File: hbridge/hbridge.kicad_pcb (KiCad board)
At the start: 2 copper layers, 53.3 x 31.8 mm, 22 parts, among them J1 CONN_A, J2 CONN_B, J3 CONN_MOTOR, J4 CONN_POWER, Q1 TIP120, Q2 TIP120, Q3 TIP120, Q4 TIP120, U1 OPTO-TRANSISTOR, U2 OPTO-TRANSISTOR

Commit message: hbridge: First PCB made
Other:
- net class Default: via_dia 1 -> 0.1; via_drill 0.1 -> 0.05
- rule via_min_drill: 0.1 -> 0.01
- rule via_min_size: 0.4 -> 0.01
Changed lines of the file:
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@@
     (links 24)
     (no_connects 0)
-    (area 0 0 0 0)
+    (area 114.070001 74.77 182.726 138.676)
     (thickness 1.6)
     (drawings 6)
@@
     (segment_width 0.2)
     (edge_width 0.15)
-    (via_size 1)
-    (via_drill 0.1)
-    (via_min_size 0.4)
-    (via_min_drill 0.1)
+    (via_size 0.1)
+    (via_drill 0.05)
+    (via_min_size 0.01)
+    (via_min_drill 0.01)
     (uvia_size 0.3)
     (uvia_drill 0.1)
@@
     (mod_text_size 1 1)
     (mod_text_width 0.15)
-    (pad_size 1.524 1.524)
-    (pad_drill 0.762)
+    (pad_size 4.064 4.064)
+    (pad_drill 0)
     (pad_to_mask_clearance 0.2)
     (aux_axis_origin 0 0)
@@
       (drillshape 0)
       (scaleselection 1)
-      (outputdirectory ""))
+      (outputdirectory ../export/))
   )
   (net 0 "")
@@
     (clearance 0.381)
     (trace_width 0.381)
-    (via_dia 1)
-    (via_drill 0.1)
+    (via_dia 0.1)
+    (via_drill 0.05)
     (uvia_dia 0.3)
     (uvia_drill 0.1)
@@
     (fp_circle (center 0 0) (end 2.6 0) (layer F.CrtYd) (width 0.05))
     (fp_circle (center 0 0) (end 0 -2.286) (layer F.SilkS) (width 0.12))
-    (pad 1 thru_hole circle (at 0 0) (size 4.064 4.064) (drill 3.2) (layers *.Cu *.Mask))
+    (pad 1 smd circle (at 0 0) (size 4.064 4.064) (layers B.Cu F.Paste F.Mask))
   )
   (module Resistors_SMD:R_1210 (layer F.Cu)
@@
   (segment (start 135.89 110.31) (end 136.07 110.31) (width 0.381) (layer F.Cu) (net 2))
   (segment (start 130.81 102.87) (end 130.81 95.25) (width 0.381) (layer F.Cu) (net 3))
-  (via (at 148.59 95.25) (size 1) (drill 0.1) (layers F.Cu B.Cu) (net 3) (status 30))
+  (via (at 148.59 95.25) (size 0.1) (drill 0.05) (layers F.Cu B.Cu) (net 3) (status 30))
   (segment (start 148.59 95.25) (end 152.4 95.25) (width 0.381) (layer F.Cu) (net 3) (status 10))
   (segment (start 130.81 95.25) (end 140.97 95.25) (width 0.381) (layer F.Cu) (net 3))
   (segment (start 140.97 95.25) (end 146.05 95.25) (width 0.381) (layer F.Cu) (net 3) (status 20))
-  (via (at 146.05 95.25) (size 1) (drill 0.1) (layers F.Cu B.Cu) (net 3) (status 30))
+  (via (at 146.05 95.25) (size 0.1) (drill 0.05) (layers F.Cu B.Cu) (net 3) (status 30))
   (segment (start 146.05 95.25) (end 148.59 95.25) (width 0.381) (layer B.Cu) (net 3))
   (segment (start 135.23 102.87) (end 132.08 102.87) (width 0.381) (layer F.Cu) (net 3))
@@
   (segment (start 160.02 101.6) (end 152.4 101.6) (width 0.381) (layer F.Cu) (net 3))
   (segment (start 152.4 95.25) (end 152.4 99.06) (width 0.381) (layer F.Cu) (net 3))
-  (via (at 152.4 101.6) (size 1) (drill 0.1) (layers F.Cu B.Cu) (net 3))
+  (via (at 152.4 101.6) (size 0.1) (drill 0.05) (layers F.Cu B.Cu) (net 3))
   (segment (start 152.4 99.06) (end 152.4 101.6) (width 0.381) (layer B.Cu) (net 3))
-  (via (at 152.4 99.06) (size 1) (drill 0.1) (layers F.Cu B.Cu) (net 3))
+  (via (at 152.4 99.06) (size 0.1) (drill 0.05) (layers F.Cu B.Cu) (net 3))
   (segment (start 152.4 101.6) (end 152.58 101.6) (width 0.381) (layer F.Cu) (net 3))
   (segment (start 130.81 102.87) (end 132.08 102.87) (width 0.381) (layer F.Cu) (net 3))
@@
   (segment (start 162.56 118.09) (end 162.56 116.84) (width 0.381) (layer F.Cu) (net 3))
   (segment (start 162.56 116.84) (end 160.02 113.03) (width 0.381) (layer F.Cu) (net 3))
-  (via (at 160.02 110.49) (size 1) (drill 0.1) (layers F.Cu B.Cu) (net 3))
+  (via (at 160.02 110.49) (size 0.1) (drill 0.05) (layers F.Cu B.Cu) (net 3))
   (segment (start 160.02 113.03) (end 160.02 110.49) (width 0.381) (layer B.Cu) (net 3))
-  (via (at 160.02 113.03) (size 1) (drill 0.1) (layers F.Cu B.Cu) (net 3))
+  (via (at 160.02 113.03) (size 0.1) (drill 0.05) (layers F.Cu B.Cu) (net 3))
   (segment (start 160.02 102.87) (end 163.83 102.87) (width 0.381) (layer F.Cu) (net 3) (status 20))
   (segment (start 160.02 93.8) (end 160.02 91.44) (width 0.381) (layer F.Cu) (net 4) (status 10))
@@
   (segment (start 170.18 95.25) (end 170.18 102.87) (width 0.381) (layer F.Cu) (net 6))
   (segment (start 168.91 95.25) (end 170.18 95.25) (width 0.381) (layer F.Cu) (net 6))
-  (via (at 168.91 95.25) (size 1) (drill 0.1) (layers F.Cu B.Cu) (net 6))
+  (via (at 168.91 95.25) (size 0.1) (drill 0.05) (layers F.Cu B.Cu) (net 6))
   (segment (start 166.37 95.25) (end 168.91 95.25) (width 0.381) (layer B.Cu) (net 6))
-  (via (at 166.37 95.25) (size 1) (drill 0.1) (layers F.Cu B.Cu) (net 6))
+  (via (at 166.37 95.25) (size 0.1) (drill 0.05) (layers F.Cu B.Cu) (net 6))
   (segment (start 146.71 102.87) (end 149.86 102.87) (width 0.381) (layer F.Cu) (net 6))
   (segment (start 154.94 100.33) (end 154.94 95.25) (width 0.381) (layer F.Cu) (net 6))
@@
   (segment (start 149.86 102.87) (end 149.86 100.33) (width 0.381) (layer F.Cu) (net 6))
   (segment (start 144.78 118.09) (end 144.78 113.03) (width 0.381) (layer F.Cu) (net 6))
-  (via (at 144.78 110.49) (size 1) (drill 0.1) (layers F.Cu B.Cu) (net 6))
+  (via (at 144.78 110.49) (size 0.1) (drill 0.05) (layers F.Cu B.Cu) (net 6))
   (segment (start 144.78 113.03) (end 144.78 110.49) (width 0.381) (layer B.Cu) (net 6))
-  (via (at 144.78 113.03) (size 1) (drill 0.1) (layers F.Cu B.Cu) (net 6))
+  (via (at 144.78 113.03) (size 0.1) (drill 0.05) (layers F.Cu B.Cu) (net 6))
   (segment (start 144.78 110.49) (end 142.24 107.95) (width 0.381) (layer F.Cu) (net 6))
   (segment (start 142.24 102.87) (end 146.71 102.87) (width 0.381) (layer F.Cu) (net 6))
@@
   (segment (start 134.62 100.33) (end 134.62 96.7) (width 0.381) (layer F.Cu) (net 13))
   (segment (start 134.62 99.72) (end 135.23 100.33) (width 0.381) (layer F.Cu) (net 13))
-  (segment (start 163.17 100.33) (end 161.9 99.67) (width 0.381) (layer F.Cu) (net 14) (status 400000))
-  (segment (start 160.02 99.06) (end 160.02 96.7) (width 0.381) (layer F.Cu) (net 14) (status 800000))
+  (segment (start 163.17 100.33) (end 161.9 99.67) (width 0.381) (layer F.Cu) (net 14))
+  (segment (start 160.02 99.06) (end 160.02 96.7) (width 0.381) (layer F.Cu) (net 14))
   (segment (start 161.9 99.67) (end 160.02 99.06) (width 0.381) (layer F.Cu) (net 14))
   (segment (start 162.56 99.72) (end 163.17 100.33) (width 0.381) (layer F.Cu) (net 14) (status 30))

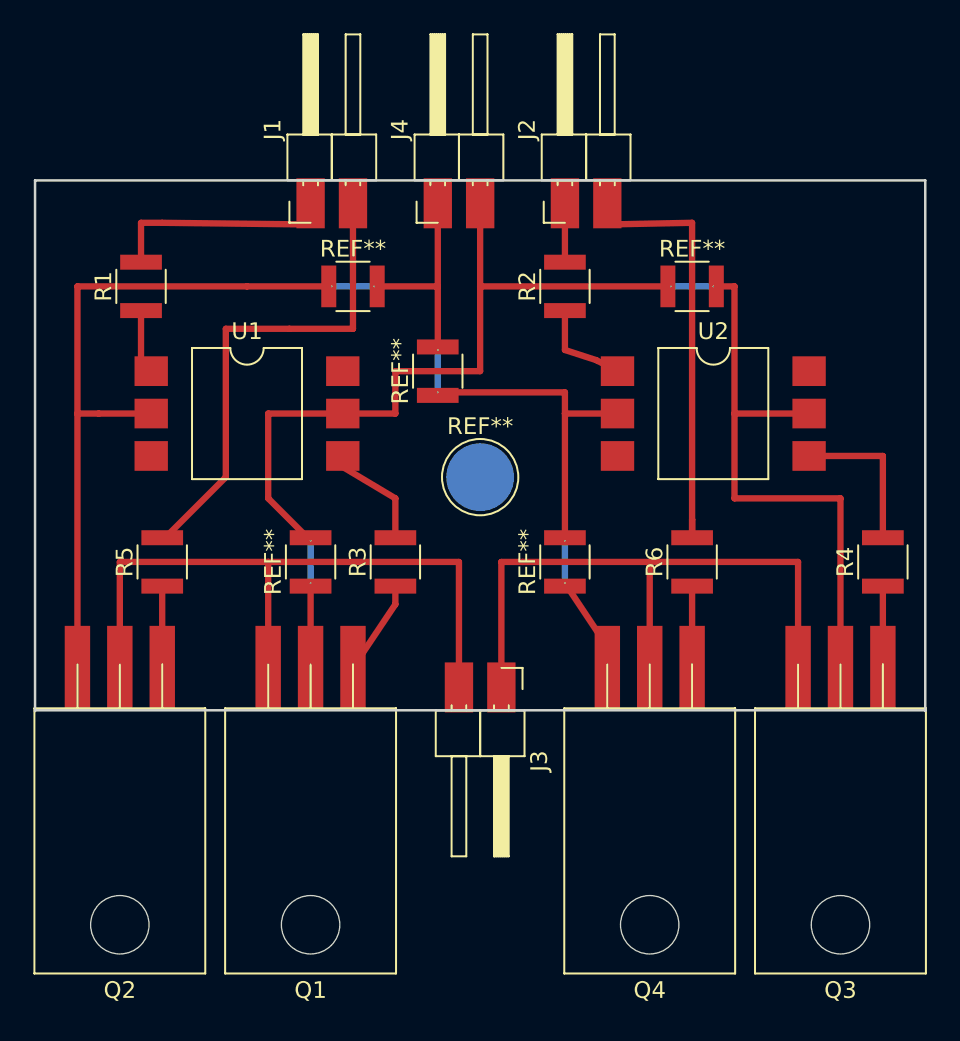
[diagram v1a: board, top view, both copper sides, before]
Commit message: hbridge: Smaller board size
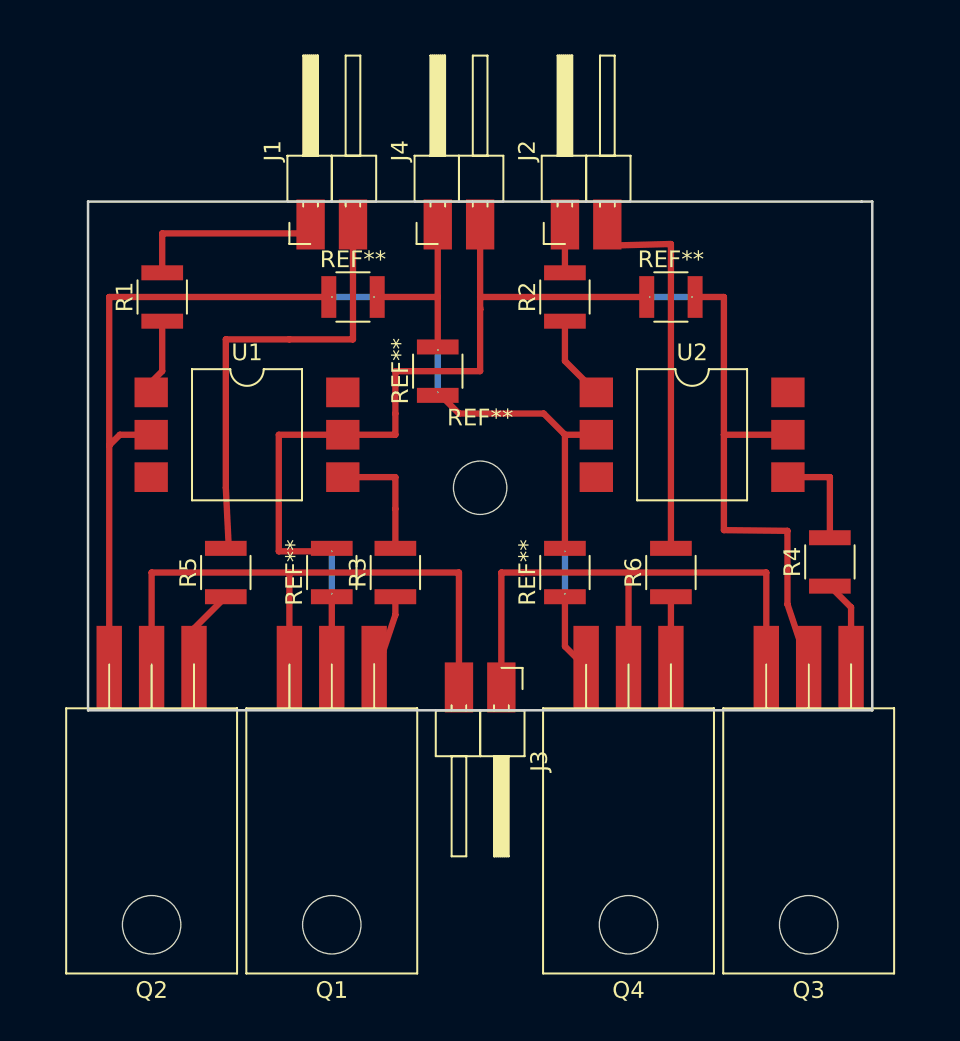
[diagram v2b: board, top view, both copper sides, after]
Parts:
- removed the REF** at (144.8, 111.8)
- removed the REF** at (160.0, 111.8)
- removed the REF** at (154.9, 106.7)
- removed the REF** at (147.3, 95.2)
- removed the REF** at (167.6, 95.2)
- added REF**: R_1210, Resistors_SMD:R_1210, F.Cu at (146.1, 112.4)
- added REF**: R_1210, Resistors_SMD:R_1210, F.Cu at (147.3, 95.9)
- added REF**: R_1210, Resistors_SMD:R_1210, F.Cu at (166.4, 95.9)
- added REF**: R_1210, Resistors_SMD:R_1210, F.Cu at (160.0, 112.4)
- added REF**: MountingHole_3.2mm_M3, Mounting_Holes:MountingHole_3.2mm_M3, F.Cu at (154.9, 107.3)
- moved R5 3.86 mm to (139.7, 112.4)
- moved R4 3.17 mm to (175.9, 111.8)
- moved Q2 1.91 mm to (137.8, 116.8)
- moved Q3 1.91 mm to (177.2, 116.8)
- moved U2 1.80 mm to (167.6, 104.1)
- moved R1 1.42 mm to (135.9, 95.9)
- moved R6 1.42 mm to (166.4, 112.4)
- moved Q1 1.27 mm to (148.6, 116.8)
- moved J1 1.27 mm to (144.8, 91.4)
- moved J2 1.27 mm to (160.0, 91.4)
- moved J4 1.27 mm to (152.4, 91.4)
- moved U1 1.27 mm to (141.0, 104.1)
- moved Q4 1.27 mm to (166.4, 116.8)
- moved R2 0.64 mm to (160.0, 95.9)
- moved R3 0.63 mm to (149.9, 112.4)
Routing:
- net Earth: track 89.2 -> 79.9 mm
- net VPP: track 90.5 -> 86.5 mm
- net Net-(R4-Pad2): track 9.50 -> 6.33 mm
- net /Sheet597E2FB2/BL: track 25.2 -> 22.2 mm
- net /Sheet597E2FB2/AL: track 29.3 -> 27.2 mm
- net /Sheet597E2FB2/OUTB: track 38.0 -> 36.1 mm
- net /Sheet597E2FB2/OUTA: track 40.5 -> 38.6 mm
- net Net-(R3-Pad2): track 6.87 -> 8.25 mm
- net /Sheet597E2FB2/AH: track 12.5 -> 11.5 mm
- net Net-(R1-Pad1): track 5.10 -> 6.01 mm
- net Net-(R2-Pad1): track 6.63 -> 5.91 mm
- net Net-(Q1-Pad1): track 5.65 -> 5.09 mm
- net /Sheet597E2FB2/BH: track 2.46 -> 3.00 mm
- net Net-(Q3-Pad1): track 4.88 -> 5.41 mm
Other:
- board size 53.3 x 31.8 mm -> 47 x 30.5 mm
